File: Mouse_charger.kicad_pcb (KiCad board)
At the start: 2 copper layers, 48 x 12.2 mm, 17 parts, among them CON1 AAA_Bat_PC_con, CON2 Molex_105133-0011, CON3 1.5mm_PTH, CON4 AAA_Bat_PC_con, U1 MCP73831-2ACI/OT, U2 MCP1700-3002E/MB

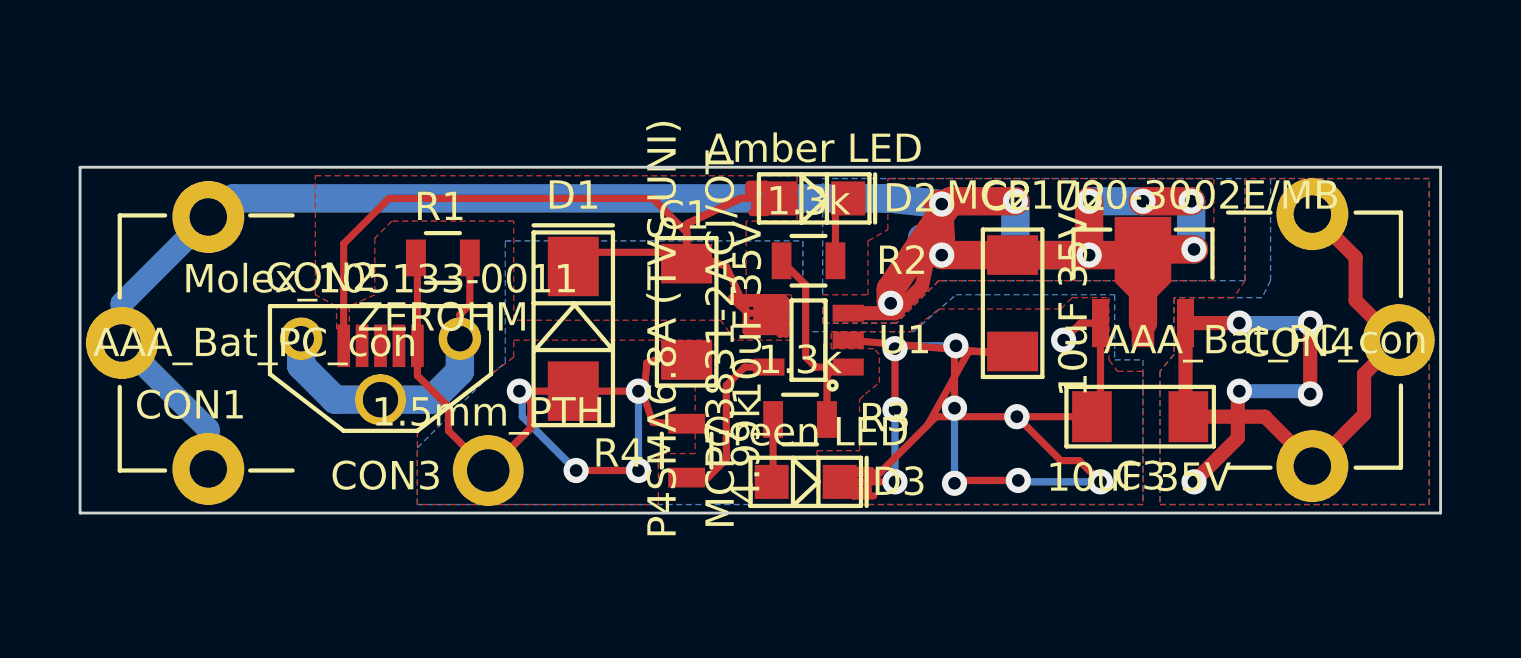
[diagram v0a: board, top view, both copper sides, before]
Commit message: Narrow outline
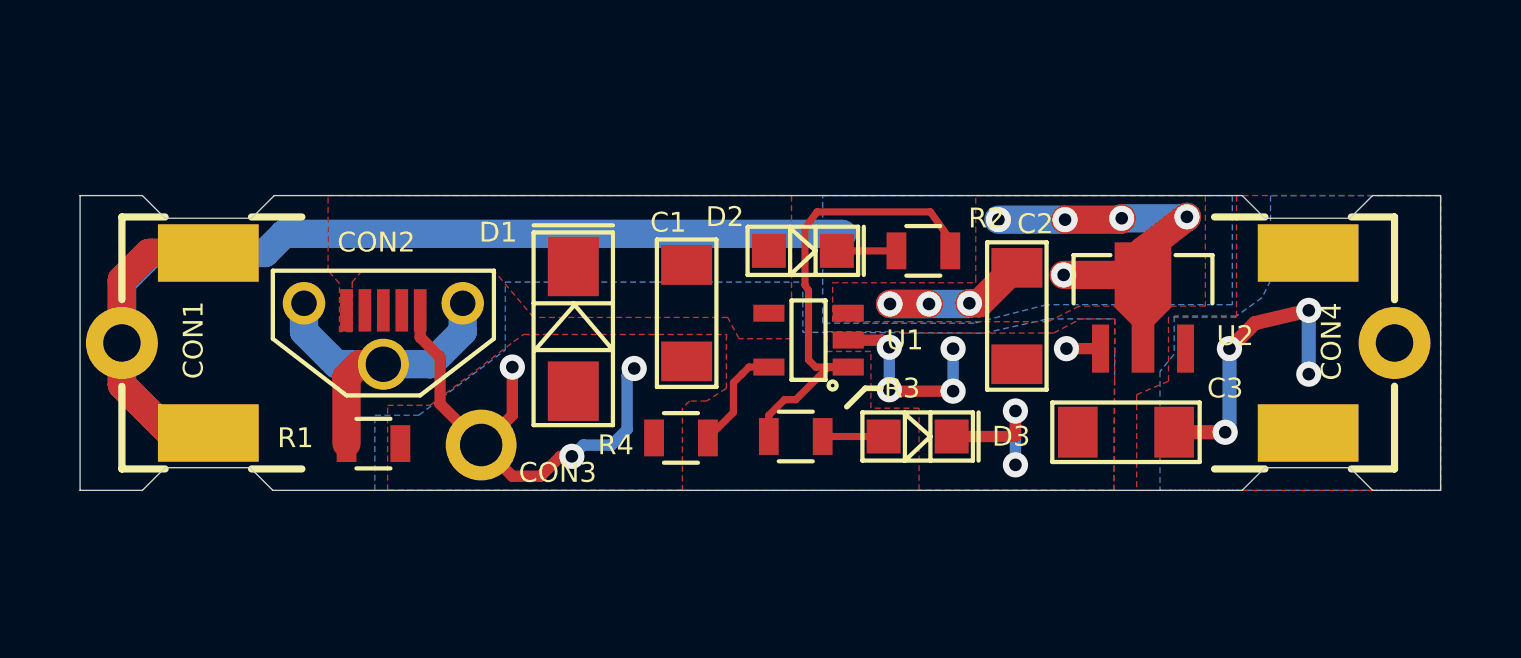
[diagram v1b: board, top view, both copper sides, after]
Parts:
- CON1, CON4: footprint Nightmechanic_PCB:Keystone_597 -> Nightmechanic_PCB:Keystone_597_narrow
- moved VAL 19.7 mm to (134.4, 100.3)
- moved R1 6.99 mm to (107.3, 103.5), turned to 180 degrees
- moved D3 4.26 mm to (126.5, 103.3)
- moved R2 4.07 mm to (126.8, 96.8), turned to 0 degrees
- moved D2 1.89 mm to (122.5, 96.8)
- moved CON2 1.25 mm to (107.7, 98.8)
- moved CON3 0.93 mm to (111.2, 103.6)
- moved U2 0.90 mm to (134.5, 98.2)
- moved C3 0.74 mm to (133.9, 103.2)
- moved R3 0.62 mm to (122.2, 103.3), turned to 0 degrees
- moved R4 0.49 mm to (118.2, 103.3), turned to 180 degrees
- moved C2 0.47 mm to (130.1, 99.0)
- moved CON4 0.18 mm to (141.8, 100.0)
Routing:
- net GND: track 89.7 -> 30.6 mm, vias 14 -> 10
- net /V_bus: track 53.4 -> 0.00 mm
- net /V_3V0: track 33.3 -> 10.3 mm, vias 5 -> 4
- net Net-(R2-Pad2): track 7.82 -> 16.8 mm
- net /V_batt: track 80.4 -> 75.2 mm, vias 9 -> 8
- net Net-(R4-Pad1): track 6.04 -> 3.80 mm
- net Net-(CON2-PadS_1): track 11.7 -> 12.4 mm
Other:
- board size 48 x 12.2 mm -> 48 x 10.4 mm
- net class gnd added: clearance 0.2, trace_width 0.4, via_dia 0.889, via_drill 0.635
- board text added: "© Magic Mouse Charger V1.0 Jan 2015"
- board text removed: "Magic Mouse Charger V1.0 Jan 2015 ©"
